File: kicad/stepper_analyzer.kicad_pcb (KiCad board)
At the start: 2 copper layers, 102 x 57 mm, 23 parts, among them J1 Connector_Conn_01x04_Male, J2 Connector_Conn_01x04_Male, M1 Motor, Q1 AO3400A, U1 ACS70331EOLCTR-2P5B3, U2 ACS70331EOLCTR-2P5B3, U3 Pico

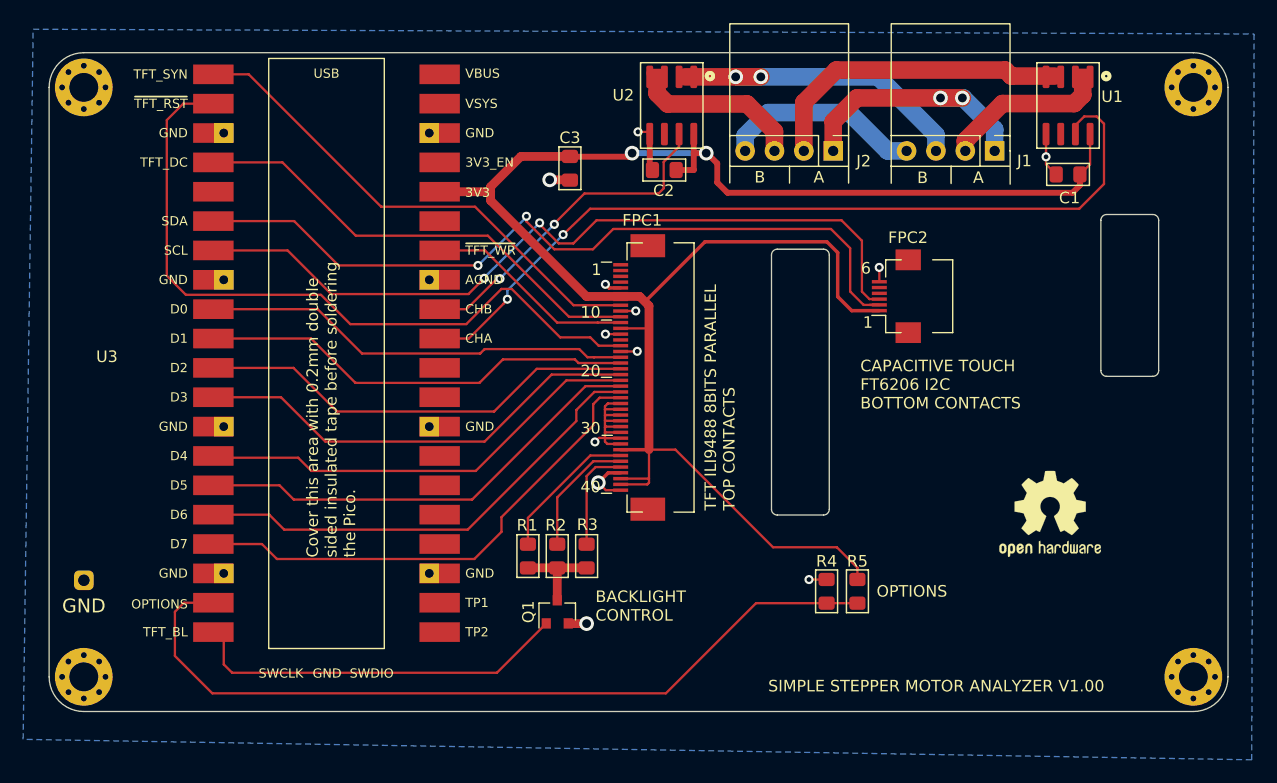
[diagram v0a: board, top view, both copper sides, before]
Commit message: Added TMCS1100A4-Q1
added TMCS1100A4-Q1 , voltage divider for vref, jumper option for 3.3/5v, stencil8 orientation holes
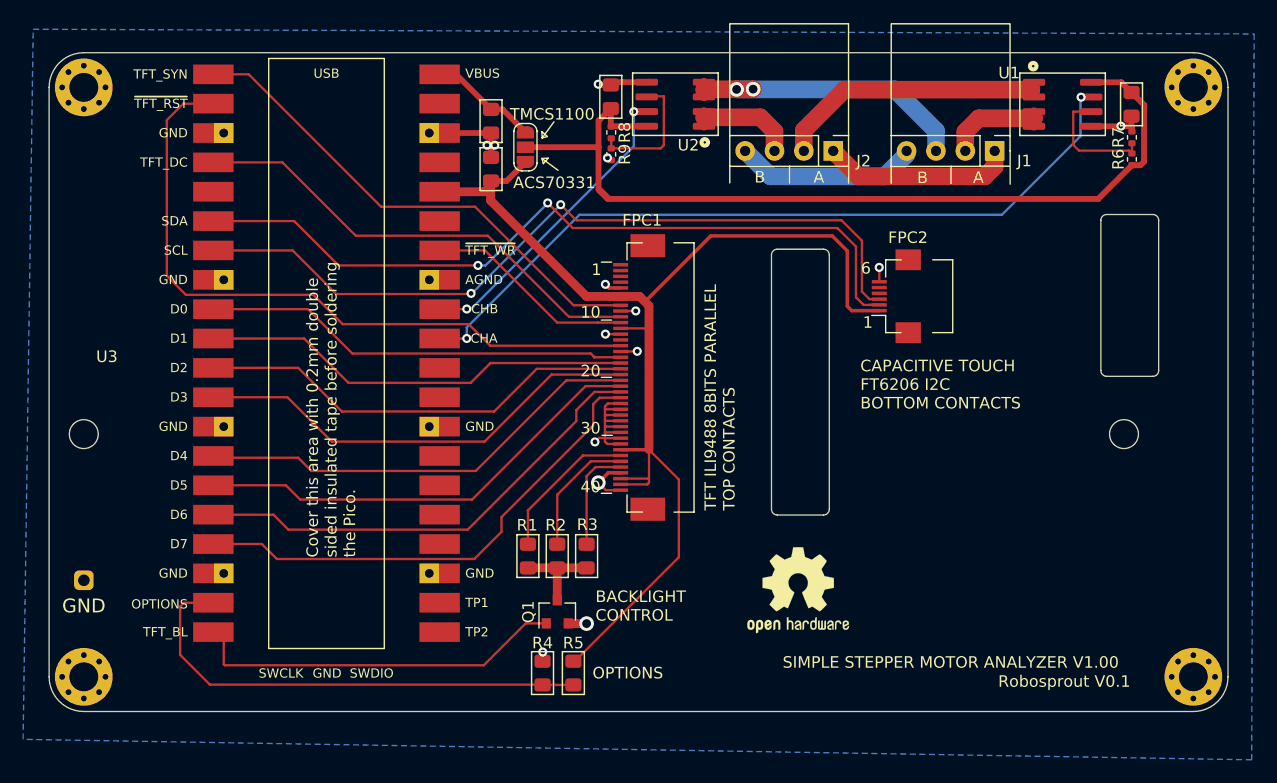
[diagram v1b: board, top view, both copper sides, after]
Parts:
- added C4: 10u, stepper_motor_analyzer:C_0805_2012Metric_Pad1.15x1.40mm_HandSolder, F.Cu at (37.2, -46.9)
- added JP1: Jumper_3_Bridged12, Jumper:SolderJumper-3_P1.3mm_Open_RoundedPad1.0x1.5mm, F.Cu at (40.2, -48.8)
- added R6: R_Small, Resistor_SMD:R_0402_1005Metric, F.Cu at (92.7, -47.8)
- added R7: R_Small, Resistor_SMD:R_0402_1005Metric, F.Cu at (92.7, -49.7)
- added R8: R_Small, Resistor_SMD:R_0402_1005Metric, F.Cu at (47.6, -50.1)
- added R9: R_Small, Resistor_SMD:R_0402_1005Metric, F.Cu at (47.6, -48.2)
- added REF**: MountingHole_2.5mm, MountingHole:MountingHole_2.5mm, F.Cu at (2.00, -24.0)
- added REF**: MountingHole_2.5mm, MountingHole:MountingHole_2.5mm, F.Cu at (92.0, -24.0)
- moved R4 25.6 mm to (41.7, -3.33)
- moved R5 25.6 mm to (44.4, -3.33)
- moved LOGO1 22.8 mm to (63.8, -10.5)
- moved C1 8.18 mm to (92.7, -52.5), turned to 90 degrees
- moved C3 7.95 mm to (37.2, -51.1)
- moved C2 7.85 mm to (47.6, -53.2), turned to -90 degrees
- moved U1 0.49 mm to (86.7, -52.5), turned to 0 degrees
- moved U2 0.33 mm to (53.2, -52.5), turned to 180 degrees
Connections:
- net /~TFT_RST renamed /~{TFT_RST}
- net /~TFT_WR renamed /~{TFT_WR}
- C1 pad 2: +3V3 -> +VSW
- C2 pad 2: +3V3 -> +VSW
- C3 pad 2: +3V3 -> +5V
- FPC1 pad 1: Net-(FPC1-Pad1) -> unconnected-(FPC1-Pad1)
- FPC1 pad 14: Net-(FPC1-Pad14) -> unconnected-(FPC1-Pad14)
- FPC1 pad 2: Net-(FPC1-Pad2) -> unconnected-(FPC1-Pad2)
- FPC1 pad 3: Net-(FPC1-Pad3) -> unconnected-(FPC1-Pad3)
- FPC1 pad 4: Net-(FPC1-Pad4) -> unconnected-(FPC1-Pad4)
- FPC2 pad 4: Net-(FPC2-Pad4) -> unconnected-(FPC2-Pad4)
- FPC2 pad 5: Net-(FPC2-Pad5) -> unconnected-(FPC2-Pad5)
- U1 pad 1: Net-(J1-Pad2) -> Net-(J2-Pad2)
- U1 pad 2: Net-(J1-Pad2) -> Net-(J2-Pad2)
- U1 pad 3: Net-(J2-Pad2) -> Net-(J1-Pad2)
- U1 pad 4: Net-(J2-Pad2) -> Net-(J1-Pad2)
- U1 pad 8: +3V3 -> +VSW
- U2 pad 1: Net-(J1-Pad3) -> Net-(J2-Pad3)
- U2 pad 2: Net-(J1-Pad3) -> Net-(J2-Pad3)
- U2 pad 3: Net-(J2-Pad3) -> Net-(J1-Pad3)
- U2 pad 4: Net-(J2-Pad3) -> Net-(J1-Pad3)
- U2 pad 8: +3V3 -> +VSW
- U3 pad 21: Net-(U3-Pad21) -> unconnected-(U3-Pad21)
- U3 pad 22: Net-(U3-Pad22) -> unconnected-(U3-Pad22)
- U3 pad 24: Net-(U3-Pad24) -> unconnected-(U3-Pad24)
- U3 pad 25: Net-(U3-Pad25) -> unconnected-(U3-Pad25)
- U3 pad 26: Net-(U3-Pad26) -> unconnected-(U3-Pad26)
- U3 pad 27: Net-(U3-Pad27) -> unconnected-(U3-Pad27)
- U3 pad 29: Net-(U3-Pad29) -> unconnected-(U3-Pad29)
- U3 pad 30: Net-(U3-Pad30) -> unconnected-(U3-Pad30)
- U3 pad 35: Net-(U3-Pad35) -> unconnected-(U3-Pad35)
- U3 pad 37: Net-(U3-Pad37) -> unconnected-(U3-Pad37)
- U3 pad 39: Net-(U3-Pad39) -> unconnected-(U3-Pad39)
- U3 pad 40: Net-(U3-Pad40) -> +5V
- U3 pad 5: Net-(U3-Pad5) -> unconnected-(U3-Pad5)
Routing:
- net +VSW: track 0.00 -> 77.5 mm
- net +3V3: track 165.2 -> 104.8 mm, vias 2 -> 0
- net /OPTIONS: track 72.0 -> 43.2 mm
- net Net-(R8-Pad2): track 0.00 -> 11.3 mm
- net Net-(U1-Pad6): track 0.00 -> 10.7 mm
- net +5V: track 0.00 -> 10.4 mm
- net GND: track 39.3 -> 46.8 mm, vias 12 -> 14
- net Net-(J1-Pad2): track 15.1 -> 9.36 mm
- net Net-(J2-Pad3): track 15.3 -> 9.57 mm
- net Net-(J1-Pad1): track 22.2 -> 16.6 mm, vias 2 -> 0
- net /CHA: track 73.4 -> 68.3 mm
- net Net-(J2-Pad2): track 27.4 -> 24.1 mm
- net /~{TFT_RST}: track 63.3 -> 60.8 mm
- net /CHB: track 29.9 -> 27.7 mm
- net Net-(J1-Pad4): track 17.5 -> 16.0 mm
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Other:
- net class Default removed
- board text added: "ACS70331"
- board text added: "Robosprout V0.1"
- board text added: "TMCS1100"
